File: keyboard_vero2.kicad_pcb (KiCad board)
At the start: 4 copper layers, 162.6 x 99.1 mm, 85 parts, among them J1 Conn_01x15_Male, SW0 SW_Push_45deg, SW1 SW_Push_45deg, SW10 SW_Push_45deg, SW11 SW_Push_45deg, SW12 SW_Push_45deg, SW13 SW_Push_45deg, SW14 SW_Push_45deg, SW15 SW_Push_45deg, SW16 SW_Push_45deg, SW17 SW_Push_45deg, SW18 SW_Push_45deg, SW19 SW_Push_45deg, SW2 SW_Push_45deg, SW20 SW_Push_45deg, SW21 SW_Push_45deg, SW22 SW_Push_45deg, SW23 SW_Push_45deg, SW24 SW_Push_45deg, SW25 SW_Push_45deg, SW26 SW_Push_45deg, SW27 SW_Push_45deg, SW28 SW_Push_45deg, SW29 SW_Push_45deg, SW3 SW_Push_45deg, SW30 SW_Push_45deg, SW31 SW_Push_45deg, SW32 SW_Push_45deg, SW33 SW_Push_45deg, SW34 SW_Push_45deg, SW35 SW_Push_45deg, SW36 SW_Push_45deg, SW37 SW_Push_45deg, SW38 SW_Push_45deg, SW39 SW_Push_45deg, SW4 SW_Push_45deg, SW40 SW_Push_45deg, SW41 SW_Push_45deg, SW42 SW_Push_45deg, SW43 SW_Push_45deg, SW44 SW_Push_45deg, SW45 SW_Push_45deg, SW46 SW_Push_45deg, SW47 SW_Push_45deg, SW48 SW_Push_45deg, SW49 SW_Push_45deg, SW5 SW_Push_45deg, SW50 SW_Push_45deg, SW51 SW_Push_45deg, SW52 SW_Push_45deg, SW53 SW_Push_45deg, SW54 SW_Push_45deg, SW55 SW_Push_45deg, SW56 SW_Push_45deg, SW57 SW_Push_45deg, SW58 SW_Push_45deg, SW59 SW_Push_45deg, SW6 SW_Push_45deg, SW60 SW_Push_45deg, SW61 SW_Push_45deg, SW62 SW_Push_45deg, SW63 SW_Push_45deg, SW7 SW_Push_45deg, SW8 SW_Push_45deg, SW9 SW_Push_45deg, U1 74LS138, U2 74LS374

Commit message: Updated schematic to match final build; created BOM
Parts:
- D1: renamed from R9; footprint Resistor_THT:R_Axial_DIN0204_L3.6mm_D1.6mm_P7.62mm_Horizontal -> Diode_THT:D_DO-35_SOD27_P7.62mm_Horizontal
- D2: renamed from R10; footprint Resistor_THT:R_Axial_DIN0204_L3.6mm_D1.6mm_P7.62mm_Horizontal -> Diode_THT:D_DO-35_SOD27_P7.62mm_Horizontal
- D3: renamed from R11; footprint Resistor_THT:R_Axial_DIN0204_L3.6mm_D1.6mm_P7.62mm_Horizontal -> Diode_THT:D_DO-35_SOD27_P7.62mm_Horizontal
- D4: renamed from R12; footprint Resistor_THT:R_Axial_DIN0204_L3.6mm_D1.6mm_P7.62mm_Horizontal -> Diode_THT:D_DO-35_SOD27_P7.62mm_Horizontal
- D5: renamed from R13; footprint Resistor_THT:R_Axial_DIN0204_L3.6mm_D1.6mm_P7.62mm_Horizontal -> Diode_THT:D_DO-35_SOD27_P7.62mm_Horizontal
- D6: renamed from R14; footprint Resistor_THT:R_Axial_DIN0204_L3.6mm_D1.6mm_P7.62mm_Horizontal -> Diode_THT:D_DO-35_SOD27_P7.62mm_Horizontal
- D7: renamed from R15; footprint Resistor_THT:R_Axial_DIN0204_L3.6mm_D1.6mm_P7.62mm_Horizontal -> Diode_THT:D_DO-35_SOD27_P7.62mm_Horizontal
- D8: renamed from R16; footprint Resistor_THT:R_Axial_DIN0204_L3.6mm_D1.6mm_P7.62mm_Horizontal -> Diode_THT:D_DO-35_SOD27_P7.62mm_Horizontal
- moved D1 7.62 mm to (86.4, 99.1), turned to 180 degrees
- moved D2 7.62 mm to (99.1, 101.6), turned to 270 degrees
- moved D3 7.62 mm to (99.1, 99.1), turned to 0 degrees
- moved D4 7.62 mm to (99.1, 96.5), turned to 0 degrees
- moved D5 7.62 mm to (99.1, 94.0), turned to 0 degrees
- moved D6 7.62 mm to (99.1, 91.4), turned to 0 degrees
- moved D7 7.62 mm to (99.1, 88.9), turned to 0 degrees
- moved D8 7.62 mm to (99.1, 86.4), turned to 0 degrees
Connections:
- D1 pad 1: Net-(R9-Pad1) -> Net-(D1-Pad1)
- D1 pad 2: Net-(R9-Pad2) -> Net-(D1-Pad2)
- D2 pad 1: Net-(R10-Pad1) -> Net-(D2-Pad1)
- D2 pad 2: Net-(R10-Pad2) -> Net-(D2-Pad2)
- D3 pad 1: Net-(R11-Pad1) -> Net-(D3-Pad1)
- D3 pad 2: Net-(R11-Pad2) -> Net-(D3-Pad2)
- D4 pad 1: Net-(R12-Pad1) -> Net-(D4-Pad1)
- D4 pad 2: Net-(R12-Pad2) -> Net-(D4-Pad2)
- D5 pad 1: Net-(R13-Pad1) -> Net-(D5-Pad1)
- D5 pad 2: Net-(R13-Pad2) -> Net-(D5-Pad2)
- D6 pad 1: Net-(R14-Pad1) -> Net-(D6-Pad1)
- D6 pad 2: Net-(R14-Pad2) -> Net-(D6-Pad2)
- D7 pad 1: Net-(R15-Pad1) -> Net-(D7-Pad1)
- D7 pad 2: Net-(R15-Pad2) -> Net-(D7-Pad2)
- D8 pad 1: Net-(R16-Pad1) -> Net-(D8-Pad1)
- D8 pad 2: Net-(R16-Pad2) -> Net-(D8-Pad2)
- SW0 pad 2: Net-(R9-Pad1) -> Net-(D1-Pad2)
- SW1 pad 2: Net-(R9-Pad1) -> Net-(D1-Pad2)
- SW10 pad 2: Net-(R10-Pad1) -> Net-(D2-Pad2)
- SW11 pad 2: Net-(R10-Pad1) -> Net-(D2-Pad2)
- SW12 pad 2: Net-(R10-Pad1) -> Net-(D2-Pad2)
- SW13 pad 2: Net-(R10-Pad1) -> Net-(D2-Pad2)
- SW14 pad 2: Net-(R10-Pad1) -> Net-(D2-Pad2)
- SW15 pad 2: Net-(R10-Pad1) -> Net-(D2-Pad2)
- SW16 pad 2: Net-(R11-Pad1) -> Net-(D3-Pad2)
- SW17 pad 2: Net-(R11-Pad1) -> Net-(D3-Pad2)
- SW18 pad 2: Net-(R11-Pad1) -> Net-(D3-Pad2)
- SW19 pad 2: Net-(R11-Pad1) -> Net-(D3-Pad2)
- SW2 pad 2: Net-(R9-Pad1) -> Net-(D1-Pad2)
- SW20 pad 2: Net-(R11-Pad1) -> Net-(D3-Pad2)
- SW21 pad 2: Net-(R11-Pad1) -> Net-(D3-Pad2)
- SW22 pad 2: Net-(R11-Pad1) -> Net-(D3-Pad2)
- SW23 pad 2: Net-(R11-Pad1) -> Net-(D3-Pad2)
- SW24 pad 2: Net-(R12-Pad1) -> Net-(D4-Pad2)
- SW25 pad 2: Net-(R12-Pad1) -> Net-(D4-Pad2)
- SW26 pad 2: Net-(R12-Pad1) -> Net-(D4-Pad2)
- SW27 pad 2: Net-(R12-Pad1) -> Net-(D4-Pad2)
- SW28 pad 2: Net-(R12-Pad1) -> Net-(D4-Pad2)
- SW29 pad 2: Net-(R12-Pad1) -> Net-(D4-Pad2)
- SW3 pad 2: Net-(R9-Pad1) -> Net-(D1-Pad2)
- SW30 pad 2: Net-(R12-Pad1) -> Net-(D4-Pad2)
- SW31 pad 2: Net-(R12-Pad1) -> Net-(D4-Pad2)
- SW32 pad 2: Net-(R13-Pad1) -> Net-(D5-Pad2)
- SW33 pad 2: Net-(R13-Pad1) -> Net-(D5-Pad2)
- SW34 pad 2: Net-(R13-Pad1) -> Net-(D5-Pad2)
- SW35 pad 2: Net-(R13-Pad1) -> Net-(D5-Pad2)
- SW36 pad 2: Net-(R13-Pad1) -> Net-(D5-Pad2)
- SW37 pad 2: Net-(R13-Pad1) -> Net-(D5-Pad2)
- SW38 pad 2: Net-(R13-Pad1) -> Net-(D5-Pad2)
- SW39 pad 2: Net-(R13-Pad1) -> Net-(D5-Pad2)
- SW4 pad 2: Net-(R9-Pad1) -> Net-(D1-Pad2)
- SW40 pad 2: Net-(R14-Pad1) -> Net-(D6-Pad2)
- SW41 pad 2: Net-(R14-Pad1) -> Net-(D6-Pad2)
- SW42 pad 2: Net-(R14-Pad1) -> Net-(D6-Pad2)
- SW43 pad 2: Net-(R14-Pad1) -> Net-(D6-Pad2)
- SW44 pad 2: Net-(R14-Pad1) -> Net-(D6-Pad2)
- SW45 pad 2: Net-(R14-Pad1) -> Net-(D6-Pad2)
- SW46 pad 2: Net-(R14-Pad1) -> Net-(D6-Pad2)
- SW47 pad 2: Net-(R14-Pad1) -> Net-(D6-Pad2)
- SW48 pad 2: Net-(R15-Pad1) -> Net-(D7-Pad2)
- SW49 pad 2: Net-(R15-Pad1) -> Net-(D7-Pad2)
- SW5 pad 2: Net-(R9-Pad1) -> Net-(D1-Pad2)
- SW50 pad 2: Net-(R15-Pad1) -> Net-(D7-Pad2)
- SW51 pad 2: Net-(R15-Pad1) -> Net-(D7-Pad2)
- SW52 pad 2: Net-(R15-Pad1) -> Net-(D7-Pad2)
- SW53 pad 2: Net-(R15-Pad1) -> Net-(D7-Pad2)
- SW54 pad 2: Net-(R15-Pad1) -> Net-(D7-Pad2)
- SW55 pad 2: Net-(R15-Pad1) -> Net-(D7-Pad2)
- SW56 pad 2: Net-(R16-Pad1) -> Net-(D8-Pad2)
- SW57 pad 2: Net-(R16-Pad1) -> Net-(D8-Pad2)
- SW58 pad 2: Net-(R16-Pad1) -> Net-(D8-Pad2)
- SW59 pad 2: Net-(R16-Pad1) -> Net-(D8-Pad2)
- SW6 pad 2: Net-(R9-Pad1) -> Net-(D1-Pad2)
- SW60 pad 2: Net-(R16-Pad1) -> Net-(D8-Pad2)
- SW61 pad 2: Net-(R16-Pad1) -> Net-(D8-Pad2)
- SW62 pad 2: Net-(R16-Pad1) -> Net-(D8-Pad2)
- SW63 pad 2: Net-(R16-Pad1) -> Net-(D8-Pad2)
- SW7 pad 2: Net-(R9-Pad1) -> Net-(D1-Pad2)
- SW8 pad 2: Net-(R10-Pad1) -> Net-(D2-Pad2)
- SW9 pad 2: Net-(R10-Pad1) -> Net-(D2-Pad2)
- SWX1 pad 2: Net-(R9-Pad1) -> Net-(D1-Pad2)
- SWX3 pad 2: Net-(R9-Pad1) -> Net-(D1-Pad2)
- U1 pad 10: Net-(R11-Pad2) -> Net-(D3-Pad1)
- U1 pad 11: Net-(R12-Pad2) -> Net-(D4-Pad1)
- U1 pad 12: Net-(R13-Pad2) -> Net-(D5-Pad1)
- U1 pad 13: Net-(R14-Pad2) -> Net-(D6-Pad1)
- U1 pad 14: Net-(R15-Pad2) -> Net-(D7-Pad1)
- U1 pad 15: Net-(R16-Pad2) -> Net-(D8-Pad1)
- U1 pad 7: Net-(R9-Pad2) -> Net-(D1-Pad1)
- U1 pad 9: Net-(R10-Pad2) -> Net-(D2-Pad1)
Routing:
- net Net-(R9-Pad1): track 318.2 -> 0.00 mm, vias 12 -> 0
- net Net-(D1-Pad2): track 0.00 -> 318.2 mm, vias 0 -> 12
- net Net-(R16-Pad1): track 249.7 -> 0.00 mm, vias 13 -> 0
- net Net-(D8-Pad2): track 0.00 -> 249.7 mm, vias 0 -> 13
- net Net-(R14-Pad1): track 235.1 -> 0.00 mm, vias 12 -> 0
- net Net-(D6-Pad2): track 0.00 -> 235.1 mm, vias 0 -> 12
- net Net-(R15-Pad1): track 229.8 -> 0.00 mm, vias 13 -> 0
- net Net-(D7-Pad2): track 0.00 -> 229.8 mm, vias 0 -> 13
- net Net-(R12-Pad1): track 225.5 -> 0.00 mm, vias 12 -> 0
- net Net-(D4-Pad2): track 0.00 -> 225.5 mm, vias 0 -> 12
- net Net-(R11-Pad1): track 225.2 -> 0.00 mm, vias 16 -> 0
- net Net-(D3-Pad2): track 0.00 -> 225.2 mm, vias 0 -> 16
- net Net-(R10-Pad1): track 218.2 -> 0.00 mm, vias 13 -> 0
- net Net-(D2-Pad2): track 0.00 -> 218.2 mm, vias 0 -> 13
- net Net-(R13-Pad1): track 206.5 -> 0.00 mm, vias 13 -> 0
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
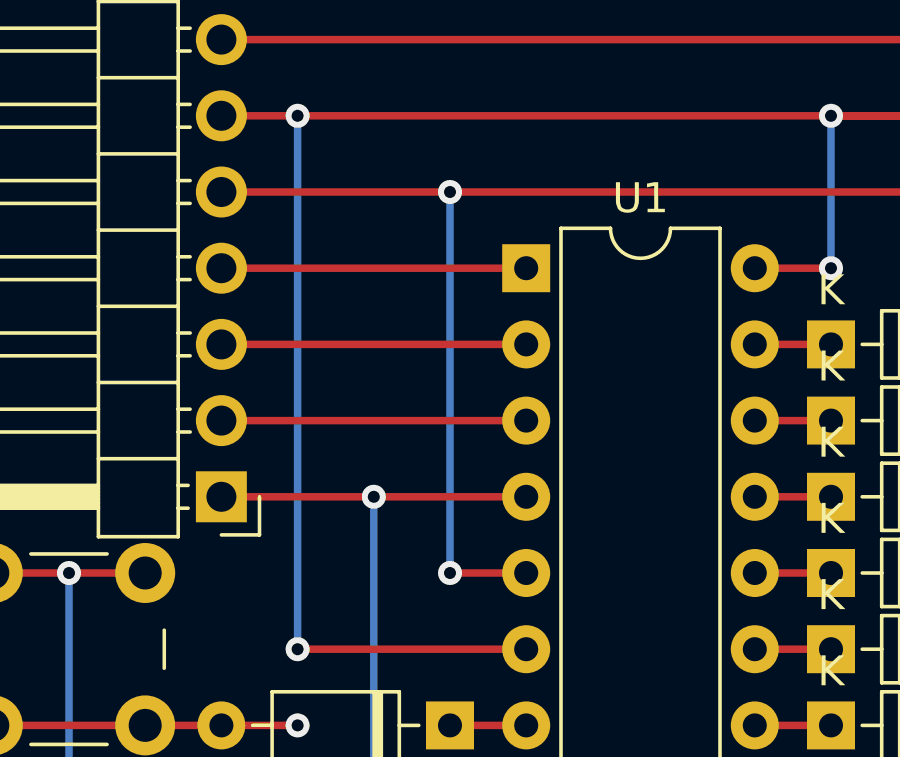
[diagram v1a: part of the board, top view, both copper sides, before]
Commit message: Unlink ~OE from LS138's enable input
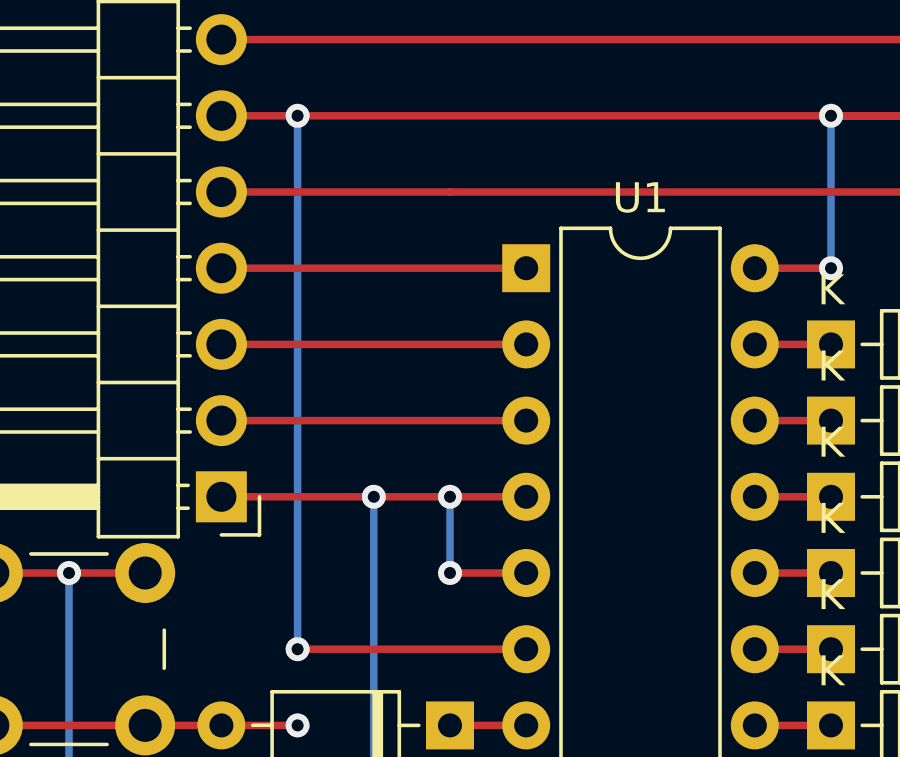
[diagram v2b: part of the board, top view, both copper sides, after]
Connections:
- J1 pad 5: /OE -> /~OE
- U1 pad 5: /OE -> GND
- U2 pad 1: /OE -> /~OE
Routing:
- net /OE: track 91.4 -> 0.00 mm, vias 2 -> 0
- net /~OE: track 0.00 -> 76.2 mm
- net GND: track 94.0 -> 99.1 mm, vias 4 -> 6
